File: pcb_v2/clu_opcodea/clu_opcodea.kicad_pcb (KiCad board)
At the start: 2 copper layers, 43.2 x 29.9 mm, 33 parts, among them J1 UCODE, U1 74LS00

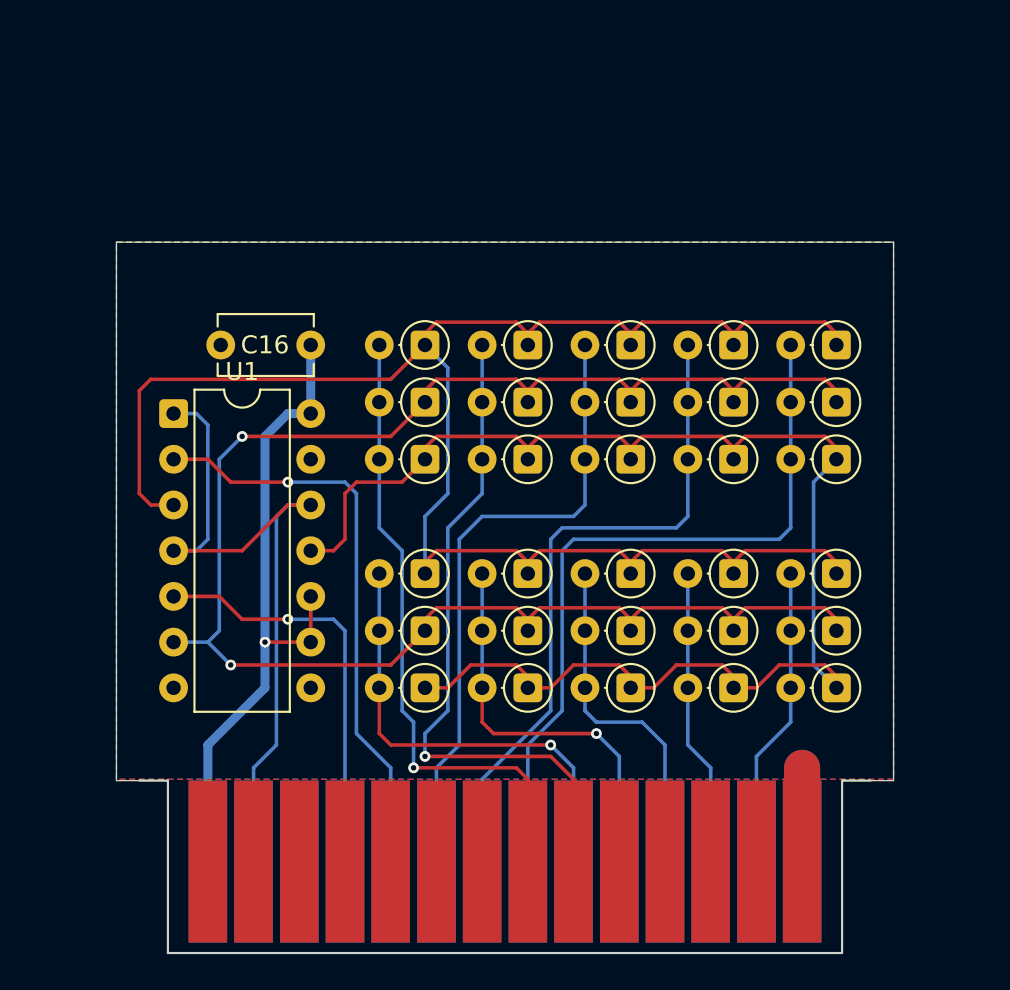
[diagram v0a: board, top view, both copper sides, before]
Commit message: continuando com a implementação da lógica de controle; ROM de ucode expandida para 17 bits
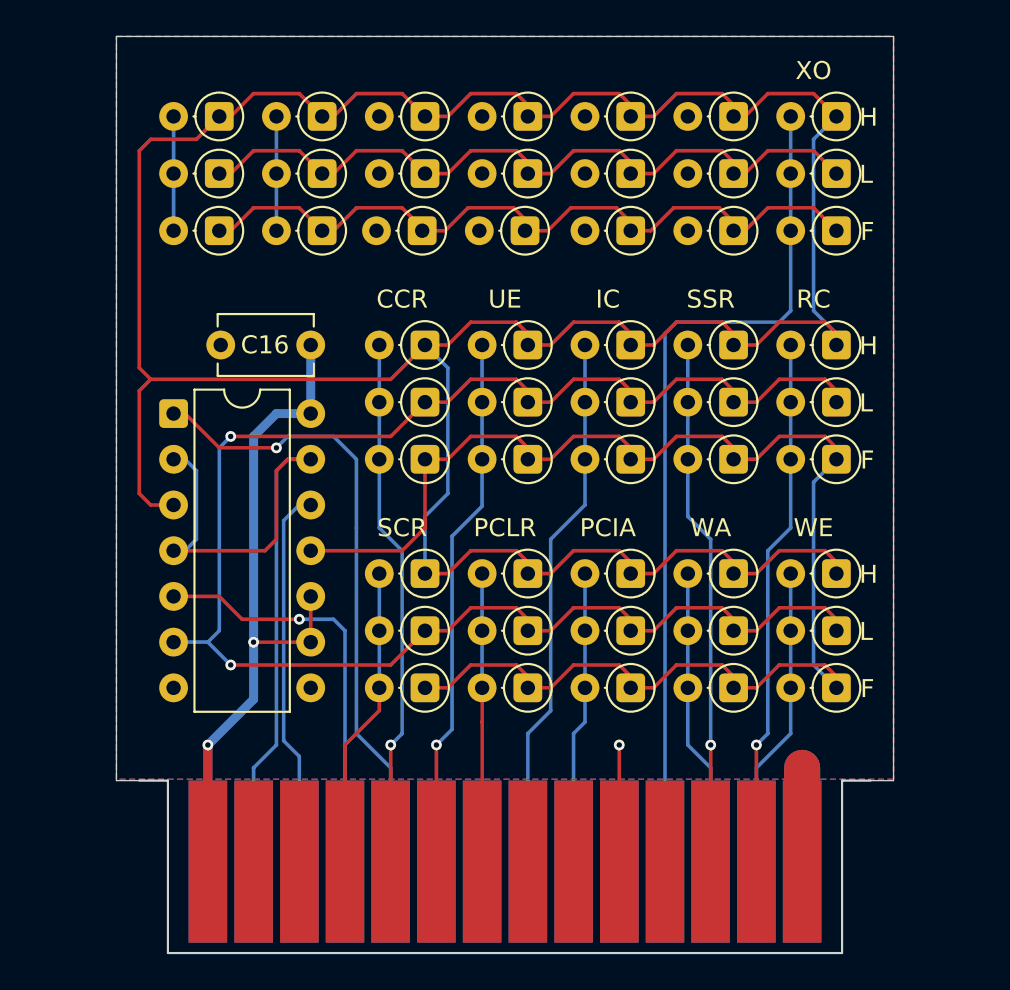
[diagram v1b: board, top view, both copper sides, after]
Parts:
- added D31: 1N4148, Diode_THT:D_DO-35_SOD27_P2.54mm_Vertical_AnodeUp, F.Cu at (89.5, 54.0)
- added D32: 1N4148, Diode_THT:D_DO-35_SOD27_P2.54mm_Vertical_AnodeUp, F.Cu at (89.5, 50.8)
- added D33: 1N4148, Diode_THT:D_DO-35_SOD27_P2.54mm_Vertical_AnodeUp, F.Cu at (89.5, 47.6)
- added D34: 1N4148, Diode_THT:D_DO-35_SOD27_P2.54mm_Vertical_AnodeUp, F.Cu at (83.8, 54.0)
- added D35: 1N4148, Diode_THT:D_DO-35_SOD27_P2.54mm_Vertical_AnodeUp, F.Cu at (83.8, 50.8)
- added D36: 1N4148, Diode_THT:D_DO-35_SOD27_P2.54mm_Vertical_AnodeUp, F.Cu at (83.8, 47.6)
- added D37: 1N4148, Diode_THT:D_DO-35_SOD27_P2.54mm_Vertical_AnodeUp, F.Cu at (78.1, 54.0)
- added D38: 1N4148, Diode_THT:D_DO-35_SOD27_P2.54mm_Vertical_AnodeUp, F.Cu at (78.1, 50.8)
- added D39: 1N4148, Diode_THT:D_DO-35_SOD27_P2.54mm_Vertical_AnodeUp, F.Cu at (78.1, 47.6)
- added D40: 1N4148, Diode_THT:D_DO-35_SOD27_P2.54mm_Vertical_AnodeUp, F.Cu at (72.2, 54.0)
- added D41: 1N4148, Diode_THT:D_DO-35_SOD27_P2.54mm_Vertical_AnodeUp, F.Cu at (72.4, 50.8)
- added D42: 1N4148, Diode_THT:D_DO-35_SOD27_P2.54mm_Vertical_AnodeUp, F.Cu at (72.4, 47.6)
- added D43: 1N4148, Diode_THT:D_DO-35_SOD27_P2.54mm_Vertical_AnodeUp, F.Cu at (66.5, 54.0)
- added D44: 1N4148, Diode_THT:D_DO-35_SOD27_P2.54mm_Vertical_AnodeUp, F.Cu at (66.7, 47.6)
- added D45: 1N4148, Diode_THT:D_DO-35_SOD27_P2.54mm_Vertical_AnodeUp, F.Cu at (66.7, 50.8)
- added D46: 1N4148, Diode_THT:D_DO-35_SOD27_P2.54mm_Vertical_AnodeUp, F.Cu at (61.0, 54.0)
- added D47: 1N4148, Diode_THT:D_DO-35_SOD27_P2.54mm_Vertical_AnodeUp, F.Cu at (61.0, 50.8)
- added D48: 1N4148, Diode_THT:D_DO-35_SOD27_P2.54mm_Vertical_AnodeUp, F.Cu at (61.0, 47.6)
- added D49: 1N4148, Diode_THT:D_DO-35_SOD27_P2.54mm_Vertical_AnodeUp, F.Cu at (55.2, 54.0)
- added D50: 1N4148, Diode_THT:D_DO-35_SOD27_P2.54mm_Vertical_AnodeUp, F.Cu at (55.2, 50.8)
- added D51: 1N4148, Diode_THT:D_DO-35_SOD27_P2.54mm_Vertical_AnodeUp, F.Cu at (55.2, 47.6)
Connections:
- D22 pad 2: ~{UC_int_cycle} -> ~{UC_int_ready}
- D23 pad 2: ~{UC_int_cycle} -> ~{UC_int_ready}
- D24 pad 2: ~{UC_int_cycle} -> ~{UC_int_ready}
- J1 pad 10: unconnected-(J1-Pin_10-Pad10) -> ~{UC_F}
- J1 pad 12: unconnected-(J1-Pin_12-Pad12) -> ~{UC_save_src_reg}
- J1 pad 13: unconnected-(J1-Pin_13-Pad13) -> ~{UC_restart_cycle}
- J1 pad 16: select_opcode_0 -> select_opcode
- J1 pad 2: unconnected-(J1-Pin_2-Pad2) -> ~{UC_A}
- J1 pad 20: ~{UC_int_cycle} -> ~{UC_D}
- J1 pad 21: ~{UC_save_src_reg} -> unconnected-(J1-Pin_21-Pad21)
- J1 pad 22: ~{UC_restart_cycle} -> ~{UC_int_ready}
- J1 pad 23: ~{UC_save_cond_reg} -> ~{UC_pcia_swap}
- J1 pad 24: ~{UC_pclr_swap} -> unconnected-(J1-Pin_24-Pad24)
- J1 pad 25: ~{UC_pcia_swap} -> ~{UC_extended_opcode}
- J1 pad 3: unconnected-(J1-Pin_3-Pad3) -> ~{UC_E}
- J1 pad 4: unconnected-(J1-Pin_4-Pad4) -> ~{UC_save_cond_reg}
- J1 pad 5: unconnected-(J1-Pin_5-Pad5) -> ~{UC_clear_cond_reg}
- J1 pad 6: unconnected-(J1-Pin_6-Pad6) -> ~{UC_ula_enable}
- J1 pad 7: unconnected-(J1-Pin_7-Pad7) -> ~{UC_pclr_swap}
- J1 pad 8: ~{UC_clear_cond_reg} -> ~{UC_C}
- J1 pad 9: ~{UC_ula_enable} -> ~{UC_B}
- U1 pad 1: select_opcode_0 -> high_cycle
- U1 pad 12: select_opcode_0 -> fetch_cycle
- U1 pad 13: fetch_cycle -> select_opcode
- U1 pad 2: high_cycle -> select_opcode
- U1 pad 4: select_opcode_0 -> select_opcode
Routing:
- net Net-(D1-K): track 85.0 -> 161.2 mm
- net Net-(D12-K): track 98.7 -> 174.4 mm
- net ~{UC_extended_opcode}: track 0.00 -> 47.6 mm
- net select_opcode: track 0.00 -> 43.2 mm
- net select_opcode_0: track 41.2 -> 0.00 mm
- net ~{UC_int_cycle}: track 35.1 -> 0.00 mm
- net ~{UC_int_ready}: track 0.00 -> 30.0 mm
- net fetch_cycle: track 0.00 -> 21.2 mm
- net ~{UC_restart_cycle}: track 41.5 -> 29.5 mm, vias 0 -> 1
- net ~{UC_save_cond_reg}: track 25.7 -> 16.8 mm, vias 1 -> 0
- net ~{UC_save_src_reg}: track 37.2 -> 29.2 mm, vias 0 -> 1
- net ~{UC_ula_enable}: track 37.5 -> 29.8 mm
- net +5V: track 36.9 -> 44.4 mm, vias 1 -> 2
- net ~{UC_pclr_swap}: track 22.5 -> 16.0 mm, vias 1 -> 0
- net ~{UC_F}: track 0.00 -> 6.48 mm, vias 0 -> 1
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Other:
- board size 43.2 x 29.9 mm -> 43.2 x 41.4 mm
- board text added: "CCR"
- board text added: "F"
- board text added: "H"
- board text added: "IC"
- board text added: "L"
- board text added: "PCIA"
- board text added: "PCLR"
- board text added: "RC"
- board text added: "SCR"
- board text added: "SSR"
- board text added: "UE"
- board text added: "WA"
- board text added: "WE"
- board text added: "XO"

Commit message: alteração de layout
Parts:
- removed D43, D44, D45, D46, D47, D48, D49, D50, D51: 1N4148, Diode_THT:D_DO-35_SOD27_P2.54mm_Vertical_AnodeUp
- moved D31 35.4 mm to (61.0, 74.9), turned to 0 degrees
- moved D32 33.2 mm to (66.7, 74.9), turned to 0 degrees
- moved D33 32.2 mm to (72.4, 74.9), turned to 0 degrees
- moved D1 29.6 mm to (61.0, 71.8), turned to 0 degrees
- moved D27 27.3 mm to (91.4, 71.8), turned to 0 degrees
- moved D7 26.6 mm to (61.0, 59.1), turned to 0 degrees
- moved D2 23.3 mm to (66.7, 71.8), turned to 0 degrees
- moved D42 22.2 mm to (91.4, 59.1), turned to 0 degrees
- moved D26 20.8 mm to (85.7, 71.8), turned to 0 degrees
- moved D8 20.6 mm to (66.7, 59.1), turned to 0 degrees
- moved D12 19.7 mm to (91.4, 78.1), turned to 0 degrees
- moved D37 19.0 mm to (61.0, 62.2), turned to 0 degrees
- moved D22 17.2 mm to (61.0, 65.4), turned to 0 degrees
- moved D3 17.2 mm to (72.4, 71.8), turned to 0 degrees
- moved D36 16.5 mm to (91.4, 62.2), turned to 0 degrees
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- renumbered C16 to C1
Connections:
- D10 pad 2: ~{UC_pclr_swap} -> ~{UC_D}
- D11 pad 2: ~{UC_pclr_swap} -> ~{UC_D}
- D12 pad 2: ~{UC_pclr_swap} -> ~{UC_D}
- D34 pad 2: ~{UC_F} -> ~{UC_C}
- D35 pad 2: ~{UC_F} -> ~{UC_C}
- D36 pad 2: ~{UC_F} -> ~{UC_C}
- D37 pad 2: ~{UC_E} -> ~{UC_B}
- D38 pad 2: ~{UC_E} -> ~{UC_B}
- D39 pad 2: ~{UC_E} -> ~{UC_B}
- D40 pad 2: ~{UC_D} -> ~{UC_A}
- D41 pad 2: ~{UC_D} -> ~{UC_A}
- D42 pad 2: ~{UC_D} -> ~{UC_A}
- J1 pad 10: ~{UC_F} -> unconnected-(J1-Pin_10-Pad10)
- J1 pad 11: unconnected-(J1-Pin_11-Pad11) -> ~{UC_C}
- J1 pad 12: ~{UC_save_src_reg} -> ~{UC_restart_cycle}
- J1 pad 13: ~{UC_restart_cycle} -> ~{UC_write_address}
- J1 pad 16: select_opcode -> fetch_cycle
- J1 pad 17: fetch_cycle -> high_cycle
- J1 pad 19: high_cycle -> select_opcode
- J1 pad 2: ~{UC_A} -> unconnected-(J1-Pin_2-Pad2)
- J1 pad 20: ~{UC_D} -> ~{UC_save_cond_reg}
- J1 pad 21: unconnected-(J1-Pin_21-Pad21) -> ~{UC_write_enable}
- J1 pad 24: unconnected-(J1-Pin_24-Pad24) -> ~{UC_A}
- J1 pad 25: ~{UC_extended_opcode} -> ~{UC_save_src_reg}
- J1 pad 26: ~{UC_write_address} -> ~{UC_clear_cond_reg}
- J1 pad 27: ~{UC_write_enable} -> ~{UC_D}
- J1 pad 3: ~{UC_E} -> unconnected-(J1-Pin_3-Pad3)
- J1 pad 4: ~{UC_save_cond_reg} -> unconnected-(J1-Pin_4-Pad4)
- J1 pad 5: ~{UC_clear_cond_reg} -> unconnected-(J1-Pin_5-Pad5)
- J1 pad 6: ~{UC_ula_enable} -> ~{UC_extended_opcode}
- J1 pad 7: ~{UC_pclr_swap} -> unconnected-(J1-Pin_7-Pad7)
- J1 pad 8: ~{UC_C} -> ~{UC_ula_enable}
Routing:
- net Net-(D1-K): track 161.2 -> 64.6 mm
- net Net-(D12-K): track 174.4 -> 84.0 mm
- net ~{UC_A}: track 6.35 -> 51.3 mm
- net ~{UC_C}: track 0.00 -> 41.4 mm, vias 0 -> 1
- net ~{UC_B}: track 6.35 -> 41.4 mm, vias 0 -> 1
- net ~{UC_D}: track 0.00 -> 31.5 mm
- net ~{UC_pcia_swap}: track 16.3 -> 45.1 mm
- net Net-(D11-K): track 101.3 -> 77.7 mm, vias 2 -> 0
- net ~{UC_extended_opcode}: track 47.6 -> 28.4 mm, vias 0 -> 1
- net ~{UC_pclr_swap}: track 16.0 -> 0.00 mm
- net ~{UC_write_enable}: track 16.8 -> 31.6 mm
- net ~{UC_write_address}: track 16.5 -> 30.7 mm, vias 0 -> 1
- net ~{UC_restart_cycle}: track 29.5 -> 38.7 mm
- net ~{UC_save_cond_reg}: track 16.8 -> 25.2 mm
- net ~{UC_int_ready}: track 30.0 -> 38.2 mm
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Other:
- board size 43.2 x 41.4 mm -> 52.1 x 31.8 mm
- board text added: "IR"
- board text added: "PIS"
- board text added: "Rev.A1 fevereiro/2026"
- board text added: "UCODE"
- board text removed: "IC"
- board text removed: "PCIA"
- board text removed: "PCLR"

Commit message: revisando o ERC
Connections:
- net ~{UC_D} renamed ~{UC_read_addr_src_reg}
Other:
- board text added: "RSR"
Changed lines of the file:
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@@
 	(net 19 "unconnected-(U1-Pad8)")
 	(net 20 "~{UC_extended_opcode}")
-	(net 21 "~{UC_D}")
+	(net 21 "~{UC_read_addr_src_reg}")
 	(net 22 "~{UC_C}")
 	(net 23 "~{UC_B}")
@@
 			(layers "*.Cu" "*.Mask")
 			(remove_unused_layers no)
-			(net 21 "~{UC_D}")
+			(net 21 "~{UC_read_addr_src_reg}")
 			(pinfunction "A")
 			(pintype "passive")
@@
 			(layers "*.Cu" "*.Mask")
 			(remove_unused_layers no)
-			(net 21 "~{UC_D}")
+			(net 21 "~{UC_read_addr_src_reg}")
 			(pinfunction "A")
 			(pintype "passive")
@@
 			(layers "*.Cu" "*.Mask")
 			(remove_unused_layers no)
-			(net 21 "~{UC_D}")
+			(net 21 "~{UC_read_addr_src_reg}")
 			(pinfunction "A")
 			(pintype "passive")
@@
 			(size 9 2.14)
 			(layers "B.Cu" "B.Mask")
-			(net 21 "~{UC_D}")
+			(net 21 "~{UC_read_addr_src_reg}")
 			(pinfunction "Pin_27")
 			(pintype "passive")
@@
 		(layer "F.SilkS")
 		(effects
+			(font
+				(size 1 1)
+				(thickness 0.15)
+			)
+		)
+	)
+	(gr_text "RSR"
+		(at 77.47 78.105 90)
+		(layer "F.SilkS")
+		(effects

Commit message: novos sinais
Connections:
- net ~{UC_B} renamed ~{UC_read_mem_const}
- net ~{UC_C} renamed ~{UC_const_boot_addr}
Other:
- board text added: "CA"
- board text added: "CC"
- board text added: "MC"
- board text added: "PC"
- board text added: "SR"
- board text added: "SS"
- board text removed: "CCR"
- board text removed: "RSR"
- board text removed: "SSR"
- board text removed: "WA"

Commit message: ajuste nos sinais do microcódigo
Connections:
- net ~{UC_const_boot_addr} renamed ~{UC_B}
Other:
- board text removed: "CA"
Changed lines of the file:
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@@
 	(net 28 "unconnected-(J1-Pin_2-Pad2)")
 	(net 29 "~{UC_read_mem_const}")
-	(net 30 "~{UC_const_boot_addr}")
+	(net 30 "~{UC_B}")
 	(footprint "Diode_THT:D_DO-35_SOD27_P2.54mm_Vertical_AnodeUp"
 		(layer "F.Cu")
@@
 			(layers "*.Cu" "*.Mask")
 			(remove_unused_layers no)
-			(net 30 "~{UC_const_boot_addr}")
+			(net 30 "~{UC_B}")
 			(pinfunction "A")
 			(pintype "passive")
@@
 			(size 9 2.14)
 			(layers "F.Cu" "F.Mask")
-			(net 30 "~{UC_const_boot_addr}")
+			(net 30 "~{UC_B}")
 			(pinfunction "Pin_11")
 			(pintype "passive")
@@
 			(layers "*.Cu" "*.Mask")
 			(remove_unused_layers no)
-			(net 30 "~{UC_const_boot_addr}")
+			(net 30 "~{UC_B}")
 			(pinfunction "A")
 			(pintype "passive")
@@
 			(layers "*.Cu" "*.Mask")
 			(remove_unused_layers no)
-			(net 30 "~{UC_const_boot_addr}")
+			(net 30 "~{UC_B}")
 			(pinfunction "A")
 			(pintype "passive")
@@
 		(layer "F.SilkS")
 		(effects
-			(font
-				(size 1 1)
-				(thickness 0.15)
-			)
-		)
-	)
-	(gr_text "CA"
-		(at 77.47 62.23 90)
-		(layer "F.SilkS")
-		(effects

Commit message: novo sinal no opcode
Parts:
- U1: value 74LS00 -> 74LS32
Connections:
- net ~{UC_B} renamed ~{UC_disable_int}
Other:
- board text added: "DI"
- board text added: "Rev.A1 maio/2026"
- board text removed: "Rev.A1 fevereiro/2026"
